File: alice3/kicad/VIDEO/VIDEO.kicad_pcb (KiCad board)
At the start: 2 copper layers, 4 parts, among them SW1 SW_PUSH, U1 Propeller_P8X32A-D40, Y1 5 MHz

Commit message: Progress on video board schematic.
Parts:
- moved Y1 2.84 mm to (124.5, 83.8)
- moved SW1 2.54 mm to (78.7, 81.3)
- moved U1 1.27 mm to (88.9, 58.4)
- moved R1 1.27 mm to (78.7, 88.9)
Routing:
- net GND: track 48.1 -> 0.00 mm
- net Net-(R1-Pad2): track 22.1 -> 19.6 mm
- net Net-(U1-Pad30): track 10.9 -> 13.3 mm
- net +3V3: track 36.5 -> 34.7 mm
- added copper zone on B.Cu, net GND
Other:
- board outline added: 127 x 101.6 mm
- board text added: "RESET"
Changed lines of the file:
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@@
     (area 0 0 0 0)
     (thickness 1.6)
-    (drawings 0)
-    (tracks 25)
+    (drawings 5)
+    (tracks 15)
     (zones 0)
     (modules 4)
@@
   )
   (module Resistors_ThroughHole:Resistor_Horizontal_RM10mm (layer F.Cu)
-    (at 77.47 88.9 180)
+    (at 78.74 88.9 180)
     (descr "Resistor, Axial,  RM 10mm, 1/3W,")
     (tags "Resistor, Axial, RM 10mm, 1/3W,")
@@
       (effects (font (size 1 1) (thickness 0.15)))
     )
-    (fp_text value 10K (at 3.81 3.81 180) (layer F.Fab)
+    (fp_text value 10K (at 0 0 180) (layer F.Fab)
       (effects (font (size 1 1) (thickness 0.15)))
     )
@@
   )
   (module Buttons_Switches_ThroughHole:SW_PUSH_SMALL (layer F.Cu)
-    (at 76.2 81.28 180)
+    (at 78.74 81.28 180)
     (fp_text reference SW1 (at 0 -0.762 180) (layer F.SilkS)
       (effects (font (size 1 1) (thickness 0.15)))
     )
-    (fp_text value SW_PUSH (at 0 1.016 180) (layer F.Fab)
+    (fp_text value SW_PUSH (at 0 0 180) (layer F.Fab)
       (effects (font (size 1 1) (thickness 0.15)))
     )
@@
   )
   (module Housings_DIP:DIP-40_W25.4mm (layer F.Cu)
-    (at 88.9 57.15)
+    (at 88.9 58.42)
     (descr "40-lead dip package, row spacing 25.4 mm (1000 mils)")
     (tags "dil dip 2.54 1000")
@@
   )
   (module Crystals:Crystal_HC48-U_Vertical (layer F.Cu)
-    (at 123.19 81.28 90)
+    (at 124.46 83.82 90)
     (descr "Crystal, Quarz, HC48/U, vertical, stehend,")
     (tags "Crystal, Quarz, HC48/U, vertical, stehend,")
@@
       (net 29 "Net-(U1-Pad31)"))
   )
-  (segment (start 88.9 85.09) (end 97.79 85.09) (width 0.25) (layer F.Cu) (net 1))
-  (segment (start 105.41 77.47) (end 114.3 77.47) (width 0.25) (layer F.Cu) (net 1))
-  (segment (start 97.79 85.09) (end 105.41 77.47) (width 0.25) (layer F.Cu) (net 1))
-  (segment (start 82.55 88.9) (end 86.36 85.09) (width 0.25) (layer F.Cu) (net 1))
-  (segment (start 86.36 85.09) (end 88.9 85.09) (width 0.25) (layer F.Cu) (net 1))
-  (segment (start 72.39 83.82) (end 80.01 83.82) (width 0.25) (layer F.Cu) (net 2))
-  (segment (start 72.39 88.9) (end 72.39 83.82) (width 0.25) (layer F.Cu) (net 2))
-  (segment (start 80.01 83.82) (end 85.09 83.82) (width 0.25) (layer F.Cu) (net 2))
-  (segment (start 85.09 83.82) (end 86.36 82.55) (width 0.25) (layer F.Cu) (net 2))
-  (segment (start 86.36 82.55) (end 88.9 82.55) (width 0.25) (layer F.Cu) (net 2))
-  (segment (start 88.9 77.47) (end 97.79 77.47) (width 0.25) (layer B.Cu) (net 3))
-  (segment (start 105.41 85.09) (end 114.3 85.09) (width 0.25) (layer B.Cu) (net 3))
-  (segment (start 97.79 77.47) (end 105.41 85.09) (width 0.25) (layer B.Cu) (net 3))
-  (segment (start 88.9 77.47) (end 88.9 80.01) (width 0.25) (layer F.Cu) (net 3))
-  (segment (start 80.01 78.74) (end 85.09 78.74) (width 0.25) (layer F.Cu) (net 3))
-  (segment (start 86.36 77.47) (end 88.9 77.47) (width 0.25) (layer F.Cu) (net 3))
-  (segment (start 85.09 78.74) (end 86.36 77.47) (width 0.25) (layer F.Cu) (net 3))
-  (segment (start 72.39 78.74) (end 80.01 78.74) (width 0.25) (layer F.Cu) (net 3))
-  (segment (start 123.19 87.42934) (end 121.71934 87.42934) (width 0.25) (layer F.Cu) (net 28))
-  (segment (start 116.84 82.55) (end 114.3 82.55) (width 0.25) (layer F.Cu) (net 28))
-  (segment (start 121.71934 87.42934) (end 116.84 82.55) (width 0.25) (layer F.Cu) (net 28))
-  (segment (start 123.19 75.13066) (end 118.31066 75.13066) (width 0.25) (layer F.Cu) (net 29))
-  (segment (start 116.84 77.47) (end 114.3 80.01) (width 0.25) (layer F.Cu) (net 29))
-  (segment (start 116.84 76.60132) (end 116.84 77.47) (width 0.25) (layer F.Cu) (net 29))
-  (segment (start 118.31066 75.13066) (end 116.84 76.60132) (width 0.25) (layer F.Cu) (net 29))
+  (gr_line (start 30.48 132.08) (end 30.48 30.48) (angle 90) (layer Edge.Cuts) (width 0.15))
+  (gr_line (start 157.48 132.08) (end 30.48 132.08) (angle 90) (layer Edge.Cuts) (width 0.15))
+  (gr_line (start 157.48 30.48) (end 157.48 132.08) (angle 90) (layer Edge.Cuts) (width 0.15))
+  (gr_line (start 30.48 30.48) (end 157.48 30.48) (angle 90) (layer Edge.Cuts) (width 0.15))
+  (gr_text RESET (at 78.74 76.2) (layer F.SilkS)
+    (effects (font (size 1.5 1.5) (thickness 0.3)))
+  )
+  (segment (start 88.9 86.36) (end 86.36 86.36) (width 0.25) (layer F.Cu) (net 1) (status 400000))
+  (segment (start 86.36 86.36) (end 83.82 88.9) (width 0.25) (layer F.Cu) (net 1) (status 800000))
+  (segment (start 114.3 78.74) (end 104.14 78.74) (width 0.25) (layer F.Cu) (net 1) (status 400000))
+  (segment (start 96.52 86.36) (end 88.9 86.36) (width 0.25) (layer F.Cu) (net 1) (status 800000))
+  (segment (start 104.14 78.74) (end 96.52 86.36) (width 0.25) (layer F.Cu) (net 1))
+  (segment (start 74.93 83.82) (end 82.55 83.82) (width 0.25) (layer F.Cu) (net 2) (status C00000))
+  (segment (start 82.55 83.82) (end 88.9 83.82) (width 0.25) (layer F.Cu) (net 2) (status C00000))
+  (segment (start 73.66 88.9) (end 73.66 85.09) (width 0.25) (layer F.Cu) (net 2) (status 400000))
+  (segment (start 73.66 85.09) (end 74.93 83.82) (width 0.25) (layer F.Cu) (net 2) (status 800000))
+  (segment (start 114.3 83.82) (end 119.38 83.82) (width 0.25) (layer F.Cu) (net 28) (status 400000))
+  (segment (start 119.38 83.82) (end 124.46 88.9) (width 0.25) (layer F.Cu) (net 28) (status 800000))
+  (segment (start 124.46 88.9) (end 124.46 89.96934) (width 0.25) (layer F.Cu) (net 28) (status C00000))
+  (segment (start 114.3 81.28) (end 119.38 81.28) (width 0.25) (layer F.Cu) (net 29) (status 400000))
+  (segment (start 122.98934 77.67066) (end 124.46 77.67066) (width 0.25) (layer F.Cu) (net 29) (status 800000))
+  (segment (start 119.38 81.28) (end 122.98934 77.67066) (width 0.25) (layer F.Cu) (net 29))
+  (zone (net 3) (net_name GND) (layer B.Cu) (hatch edge 0.508)
+    (connect_pads (clearance 0.508))
+    (min_thickness 0.254)
+    (fill yes (arc_segments 16) (thermal_gap 0.508) (thermal_bridge_width 0.508))
+    (polygon
+      (pts
+        (xy 154.94 129.54) (xy 33.02 129.54) (xy 33.02 33.02) (xy 154.94 33.02) (xy 154.94 129.54)
+      )
+    )
+  )
 )

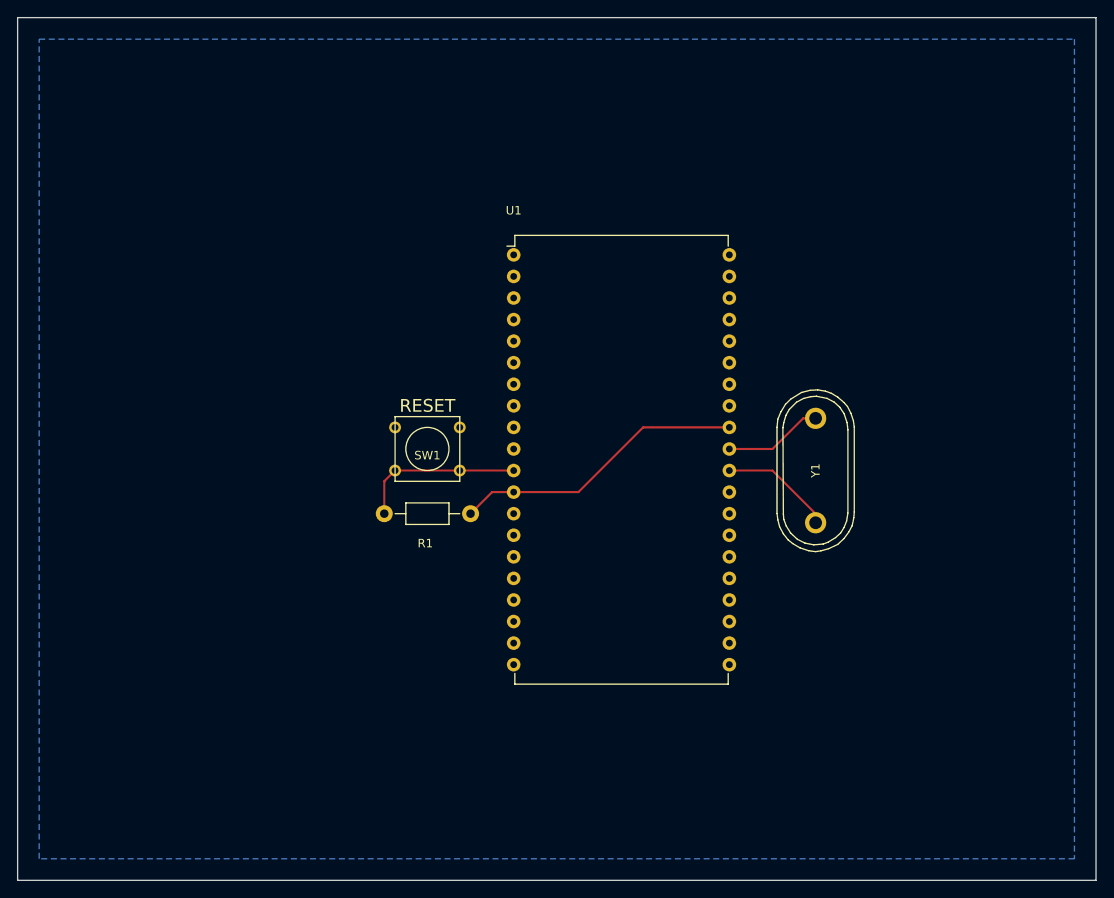
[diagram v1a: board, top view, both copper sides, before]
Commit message: Start PCB of video board.
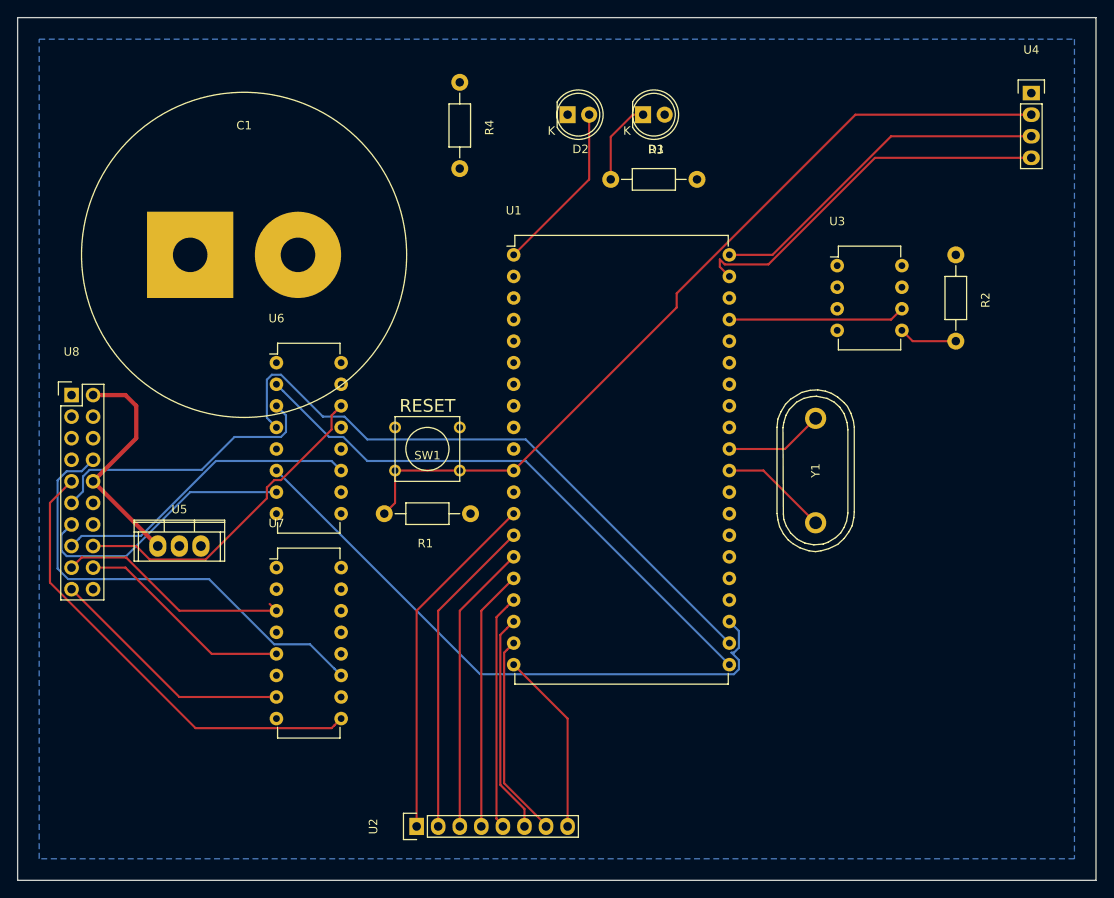
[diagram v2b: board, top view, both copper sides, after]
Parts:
- added C1: 1000 µF, Discret:CP36V, F.Cu at (57.1, 58.4)
- added D1: POWER, LEDs:LED-5MM, F.Cu at (104.1, 41.9)
- added D2: DEBUG, LEDs:LED-5MM, F.Cu at (95.2, 41.9)
- added R2: 10k, Resistors_ThroughHole:Resistor_Horizontal_RM10mm, F.Cu at (141.0, 63.5)
- added R3: 100, Resistors_ThroughHole:Resistor_Horizontal_RM10mm, F.Cu at (105.4, 49.5)
- added R4: 100, Resistors_ThroughHole:Resistor_Horizontal_RM10mm, F.Cu at (82.5, 43.2)
- added U2: VGA_daughter_board, Pin_Headers:Pin_Header_Straight_1x08, F.Cu at (77.5, 125.7)
- added U3: 24LC256, Housings_DIP:DIP-8_W7.62mm, F.Cu at (127.0, 59.7)
- added U4: Propeller_Plug, Pin_Headers:Pin_Header_Straight_1x04, F.Cu at (149.9, 39.4)
- added U5: LM2937-3.3, Power_Integrations:TO-220, F.Cu at (49.5, 92.7)
- added U6: 74HC4050, Housings_DIP:DIP-16_W7.62mm, F.Cu at (61.0, 71.1)
- added U7: 74HC4050, Housings_DIP:DIP-16_W7.62mm, F.Cu at (61.0, 95.2)
- added U8: Alice_3_bus, Pin_Headers:Pin_Header_Straight_2x10, F.Cu at (36.8, 74.9)
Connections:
- U1 pad 21: Net-(U1-Pad21) -> /D0
- U1 pad 22: Net-(U1-Pad22) -> /D1
- U1 pad 23: Net-(U1-Pad23) -> /D2
- U1 pad 24: Net-(U1-Pad24) -> /D3
- U1 pad 25: Net-(U1-Pad25) -> /D4
- U1 pad 26: Net-(U1-Pad26) -> /D5
- U1 pad 27: Net-(U1-Pad27) -> /D6
- U1 pad 28: Net-(U1-Pad28) -> /D7
- U1 pad 33: Net-(U1-Pad33) -> //IORQ
- U1 pad 34: Net-(U1-Pad34) -> //WR
- U1 pad 35: Net-(U1-Pad35) -> /A7
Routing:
- net Net-(R1-Pad2): track 19.6 -> 98.9 mm
- net /D1: track 0.00 -> 73.9 mm
- net /D2: track 0.00 -> 71.6 mm
- net /D0: track 0.00 -> 67.0 mm
- net Net-(U7-Pad9): track 0.00 -> 54.8 mm
- net Net-(U7-Pad11): track 0.00 -> 54.2 mm
- net Net-(U1-Pad39): track 0.00 -> 44.6 mm
- net Net-(U1-Pad13): track 0.00 -> 41.6 mm
- net Net-(U1-Pad40): track 0.00 -> 41.3 mm
- net Net-(U6-Pad14): track 0.00 -> 39.1 mm
- net Net-(U1-Pad14): track 0.00 -> 38.0 mm
- net Net-(U6-Pad11): track 0.00 -> 36.4 mm
- net +3V3: track 34.7 -> 0.00 mm
- net Net-(U1-Pad15): track 0.00 -> 34.4 mm
- net Net-(U6-Pad3): track 0.00 -> 33.3 mm
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
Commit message: Tighten video board PCB.
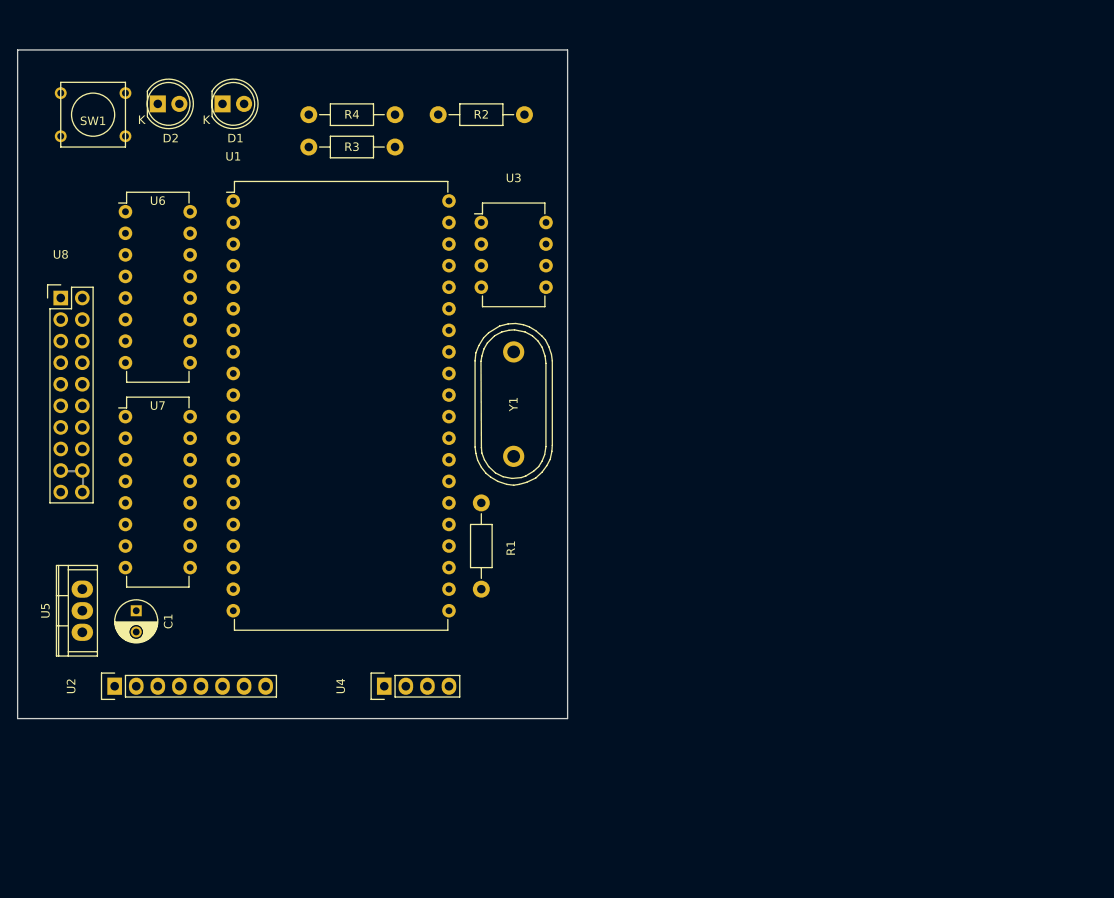
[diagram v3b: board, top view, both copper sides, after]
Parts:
- C1: footprint Discret:CP36V -> Capacitors_ThroughHole:C_Radial_D5_L6_P2.5
- SW1: value SW_PUSH -> RESET
- moved U4 103.4 mm to (73.7, 109.2), turned to 90 degrees
- moved R2 59.9 mm to (85.1, 41.9), turned to 180 degrees
- moved SW1 55.7 mm to (39.4, 41.9)
- moved D1 49.5 mm to (54.6, 40.6)
- moved D2 48.3 mm to (47.0, 40.6)
- moved C1 43.8 mm to (44.5, 100.3), turned to 270 degrees
- moved U3 42.2 mm to (85.1, 54.6)
- moved U2 39.2 mm to (41.9, 109.2)
- moved Y1 36.4 mm to (88.9, 76.0)
- moved R3 35.8 mm to (69.8, 45.7)
- moved U1 33.6 mm to (55.9, 52.1)
- moved U6 25.1 mm to (43.2, 53.3)
- moved U7 25.1 mm to (43.2, 77.5)
- moved U5 13.7 mm to (38.1, 100.3), turned to 90 degrees
- moved R4 12.8 mm to (69.8, 41.9), turned to 0 degrees
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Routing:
- net Net-(R1-Pad2): track 98.9 -> 0.00 mm
- net /D1: track 73.9 -> 0.00 mm
- net /D2: track 71.6 -> 0.00 mm
- net /D0: track 67.0 -> 0.00 mm
- net Net-(U7-Pad9): track 54.8 -> 0.00 mm
- net Net-(U7-Pad11): track 54.2 -> 0.00 mm
- net Net-(U1-Pad39): track 44.6 -> 0.00 mm
- net Net-(U1-Pad13): track 41.6 -> 0.00 mm
- net Net-(U1-Pad40): track 41.3 -> 0.00 mm
- net Net-(U6-Pad14): track 39.1 -> 0.00 mm
- net Net-(U1-Pad14): track 38.0 -> 0.00 mm
- net Net-(U6-Pad11): track 36.4 -> 0.00 mm
- net Net-(U1-Pad15): track 34.4 -> 0.00 mm
- net Net-(U6-Pad3): track 33.3 -> 0.00 mm
- net Net-(U6-Pad7): track 32.3 -> 0.00 mm
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- removed copper zone on B.Cu, net GND
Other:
- board size 127 x 101.6 mm -> 64.8 x 78.7 mm
- board text removed: "RESET"
